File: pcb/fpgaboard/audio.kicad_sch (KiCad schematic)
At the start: 25 parts, among them J26 Conn_02x05_Odd_Even, J27 Conn_02x03_Odd_Even, J28 SJ1-3533NG, U23 TDA7050, U24 TDA7050

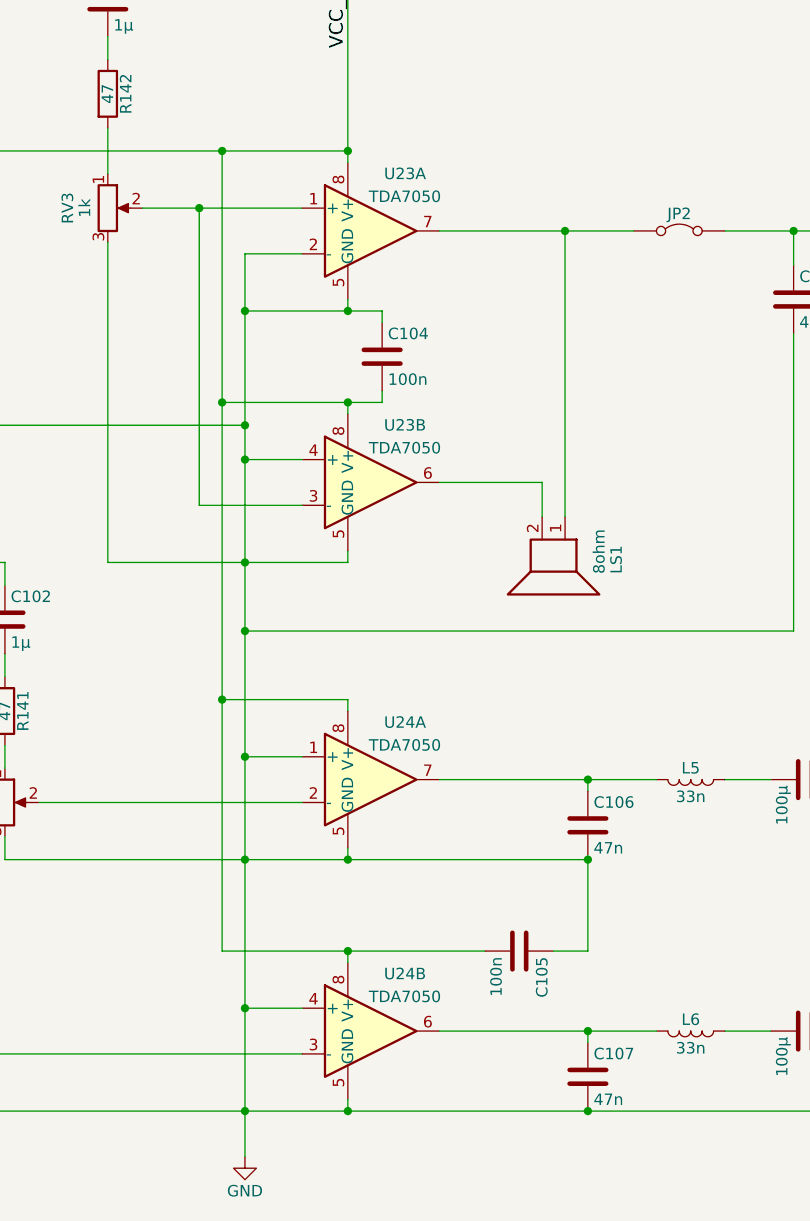
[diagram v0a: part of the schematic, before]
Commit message: Migrate other PCBs from KiCad 4 to KiCad 8
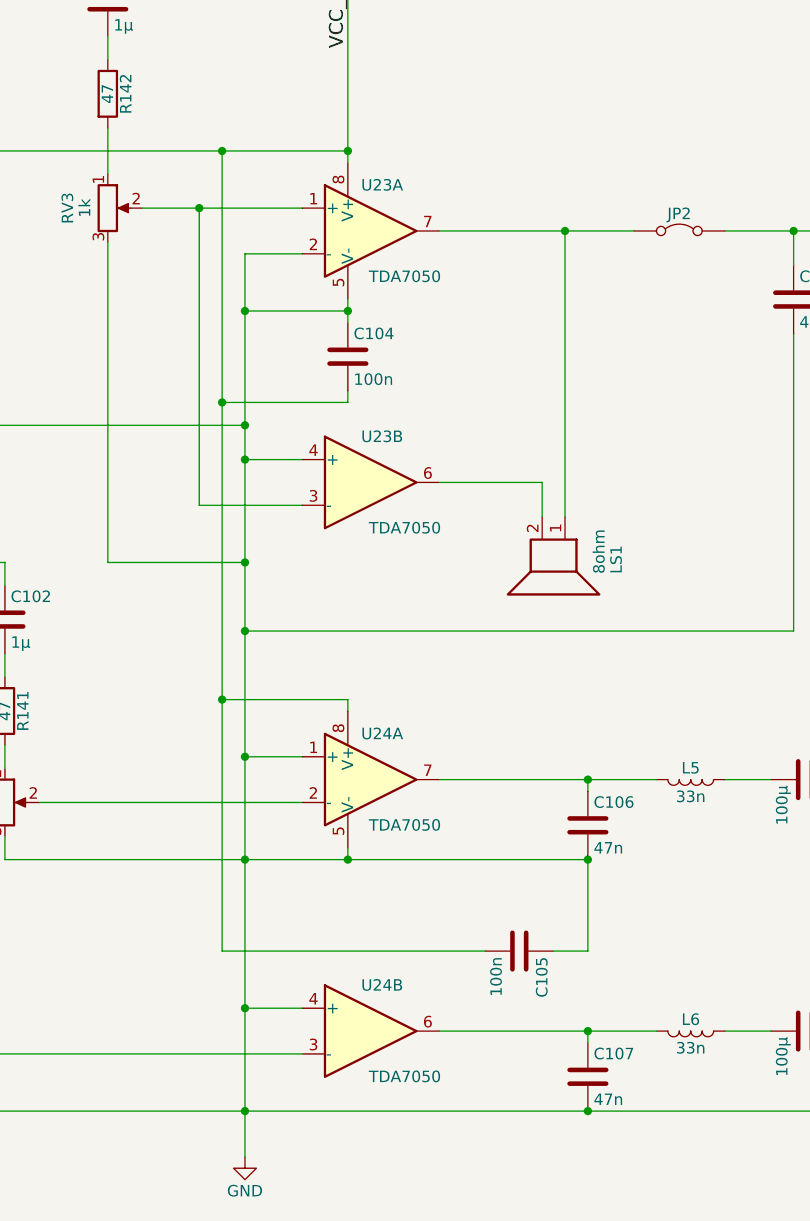
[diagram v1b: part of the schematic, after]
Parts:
- added unit 3 of U23
- added unit 3 of U24
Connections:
- net GND: now also U23.5 (V-), U24.5 (V-); no longer U23.5 (GND), U23.5 (GND), U24.5 (GND), U24.5 (GND)
- net VCC_AMP: now also U23.8 (V+), U24.8 (V+); no longer U23.8 (V+), U23.8 (V+), U24.8 (V+), U24.8 (V+)
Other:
- moved on the sheet: C104
